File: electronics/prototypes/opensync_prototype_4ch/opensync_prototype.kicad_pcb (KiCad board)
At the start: 4 copper layers, 100 x 100 mm, 86 parts, among them J1 61400416121, J12 SM03B-SRSS-TB, J13 61611042121502, J2 61611042121502, J4 61611042121502, J5 61611042121502, J6 61611042121502, J7 61611042121502, SW1 SW_Push, SW2 SW_Push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

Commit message: 4ch PCB fixup
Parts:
- moved J13 10.0 mm to (107.0, 51.0)
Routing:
- net /Microcontroller and Ext. Clock/SAFETY_INTERLOCK: track 60.2 -> 71.7 mm
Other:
- board text added: "4ch Prototype"
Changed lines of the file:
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@@
 	(footprint "61611042121502:61611042121502"
 		(layer "F.Cu")
-		(at 117 51 180)
+		(at 107 51 180)
 		(property "Reference" "J13"
-			(at -5.6 -0.1 0)
+			(at -5.8 -3.5 0)
 			(layer "F.SilkS")
 			(effects
@@
 		)
 	)
+	(gr_text "4ch Prototype"
+		(at 133.4 50.2 0)
+		(layer "F.SilkS")
+		(effects
+			(font
+				(size 2 2)
+				(thickness 0.3)
+				(bold yes)
+			)
+			(justify left bottom)
+		)
+	)
 	(gr_text "Reboot"
 		(at 65.7 104.7 0)
@@
 	)
 	(gr_text "Safety\nInterlock"
-		(at 113.2 60.8 0)
+		(at 102.8 60.2 0)
 		(layer "F.SilkS")
 		(effects
@@
 	)
 	(segment
-		(start 142 72)
-		(end 121 51)
+		(start 135.92725 92.83075)
+		(end 141.16925 92.83075)
 		(width 0.1565)
 		(layer "F.Cu")
@@
 	)
 	(segment
-		(start 135.92725 92.83075)
-		(end 141.16925 92.83075)
+		(start 135.8965 92.8)
+		(end 135.92725 92.83075)
 		(width 0.1565)
 		(layer "F.Cu")
@@
 	)
 	(segment
-		(start 142 92)
-		(end 142 72)
+		(start 107 55.1)
+		(end 107 51)
 		(width 0.1565)
 		(layer "F.Cu")
@@
 	)
 	(segment
-		(start 135.8965 92.8)
-		(end 135.92725 92.83075)
+		(start 126.6 58)
+		(end 109.9 58)
 		(width 0.1565)
 		(layer "F.Cu")
@@
 	)
 	(segment
-		(start 121 51)
-		(end 117 51)
+		(start 109.9 58)
+		(end 107 55.1)
+		(width 0.1565)
+		(layer "F.Cu")
+		(net 85)
+	)
+	(segment
+		(start 142 73.4)
+		(end 126.6 58)
+		(width 0.1565)
+		(layer "F.Cu")
+		(net 85)
+	)
+	(segment
+		(start 142 92)
+		(end 142 73.4)
 		(width 0.1565)
 		(layer "F.Cu")

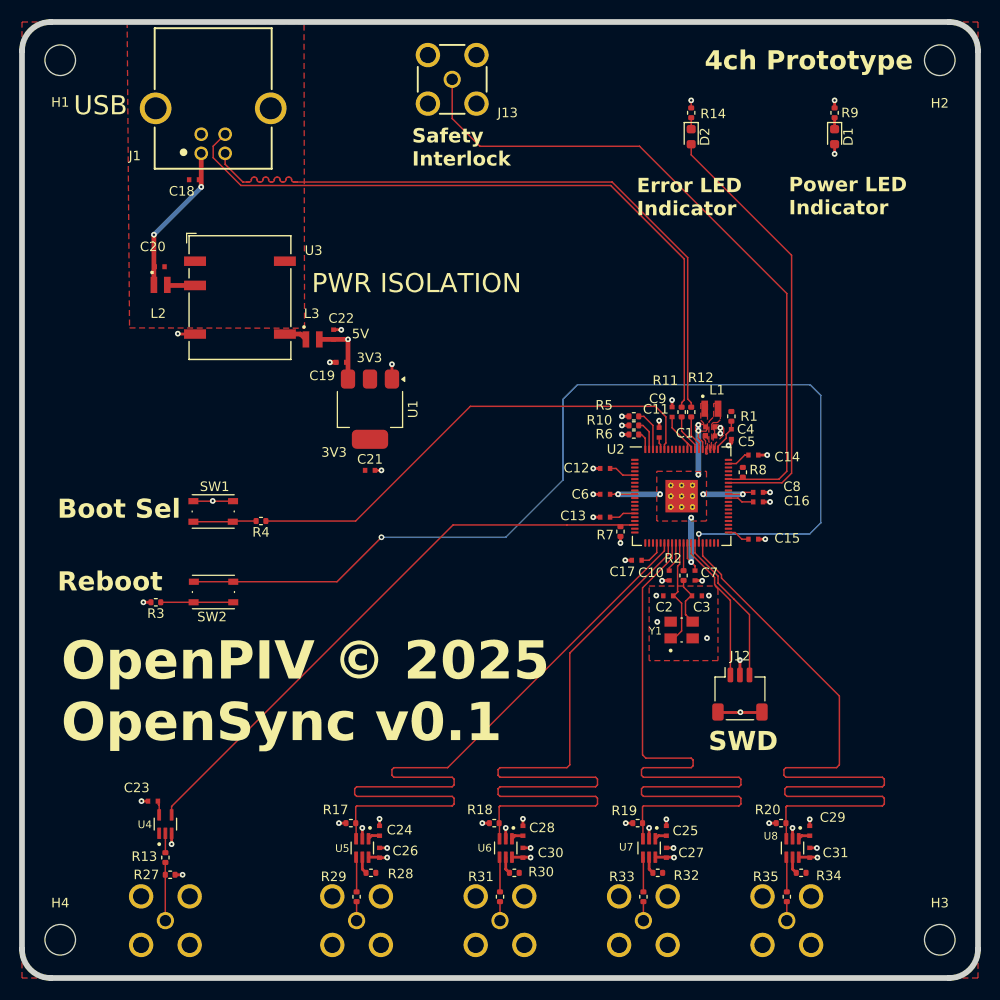
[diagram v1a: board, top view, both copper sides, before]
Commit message: Added part numbers
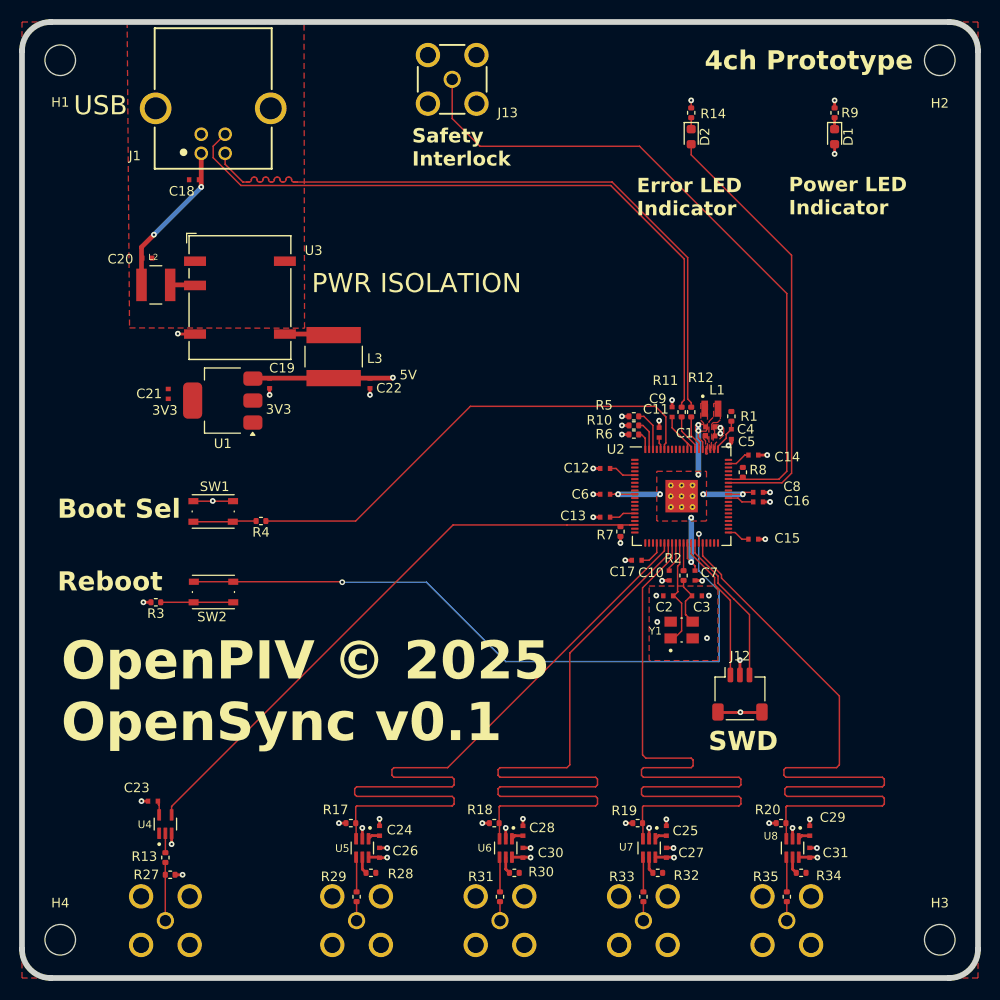
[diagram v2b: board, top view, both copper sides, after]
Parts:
- C2, C3: value C -> 15p
- L2: footprint RP2350_80QFN_minimal:L_pol_2016 -> ASPI-4030S-150M-T:IND_ASPI-4030S-150M-T
- L3: footprint RP2350_80QFN_minimal:L_pol_2016 -> ASPI6045S220MT:IND_ASPI6045S220MT
- moved C21 22.6 mm to (77.3, 83.9), turned to 90 degrees
- moved U1 15.4 mm to (83.0, 84.6), turned to 180 degrees
- moved C19 7.82 mm to (87.9, 82.8), turned to -90 degrees
- moved C22 6.36 mm to (98.4, 82.8), turned to -90 degrees
- moved L3 2.84 mm to (94.6, 80.0), turned to -90 degrees
- moved C20 1.58 mm to (75.1, 69.7)
- moved L2 0.50 mm to (76.0, 72.5)
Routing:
- net /Microcontroller and Ext. Clock/RUN: track 107.0 -> 73.6 mm
- net +5V: track 16.1 -> 23.6 mm
- net Net-(U3-+VOUT): track 2.43 -> 5.15 mm
- net GND: track 47.1 -> 44.7 mm, vias 53 -> 51
- net VBUS: track 15.8 -> 16.3 mm
